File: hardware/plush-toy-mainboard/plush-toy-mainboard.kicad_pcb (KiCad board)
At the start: 4 copper layers, 90 x 60 mm, 108 parts, among them U1 ESP32-S3-WROOM-1-N16R8

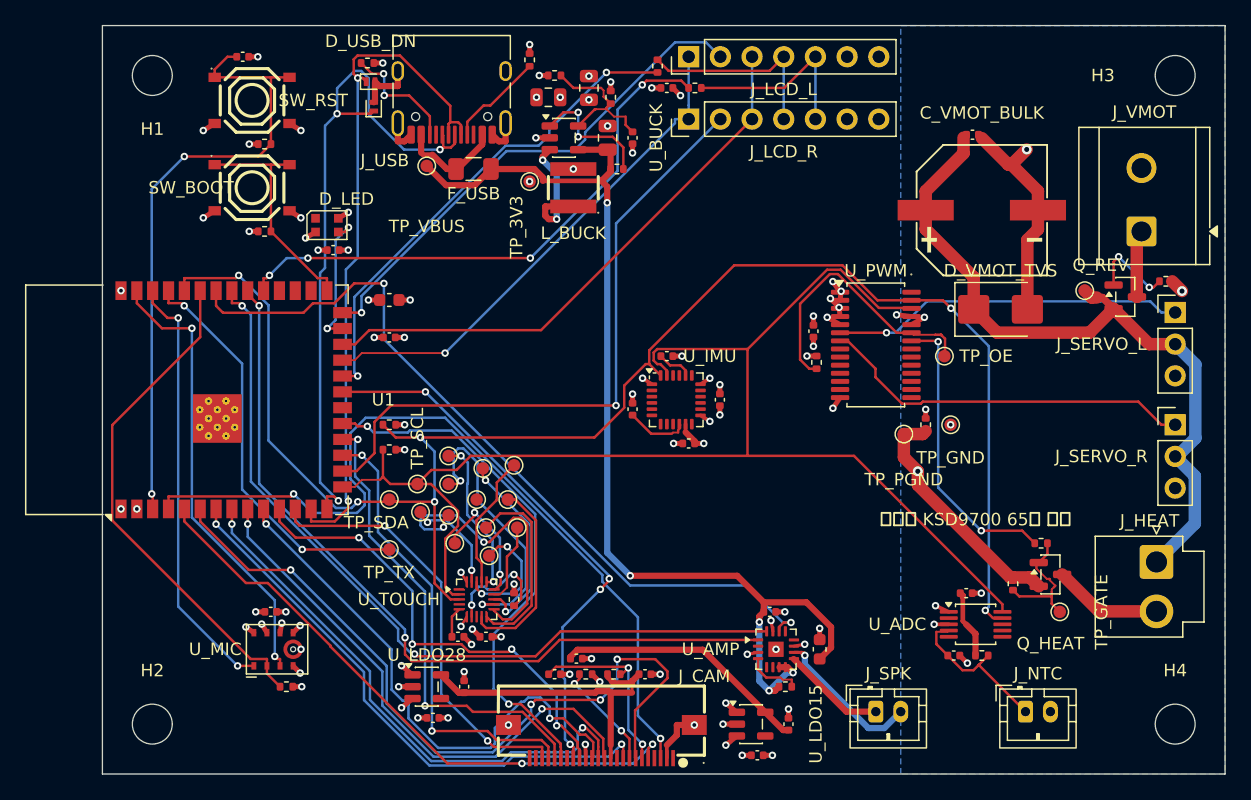
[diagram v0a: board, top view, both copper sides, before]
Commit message: feat(pcb): complete plush toy mainboard routing
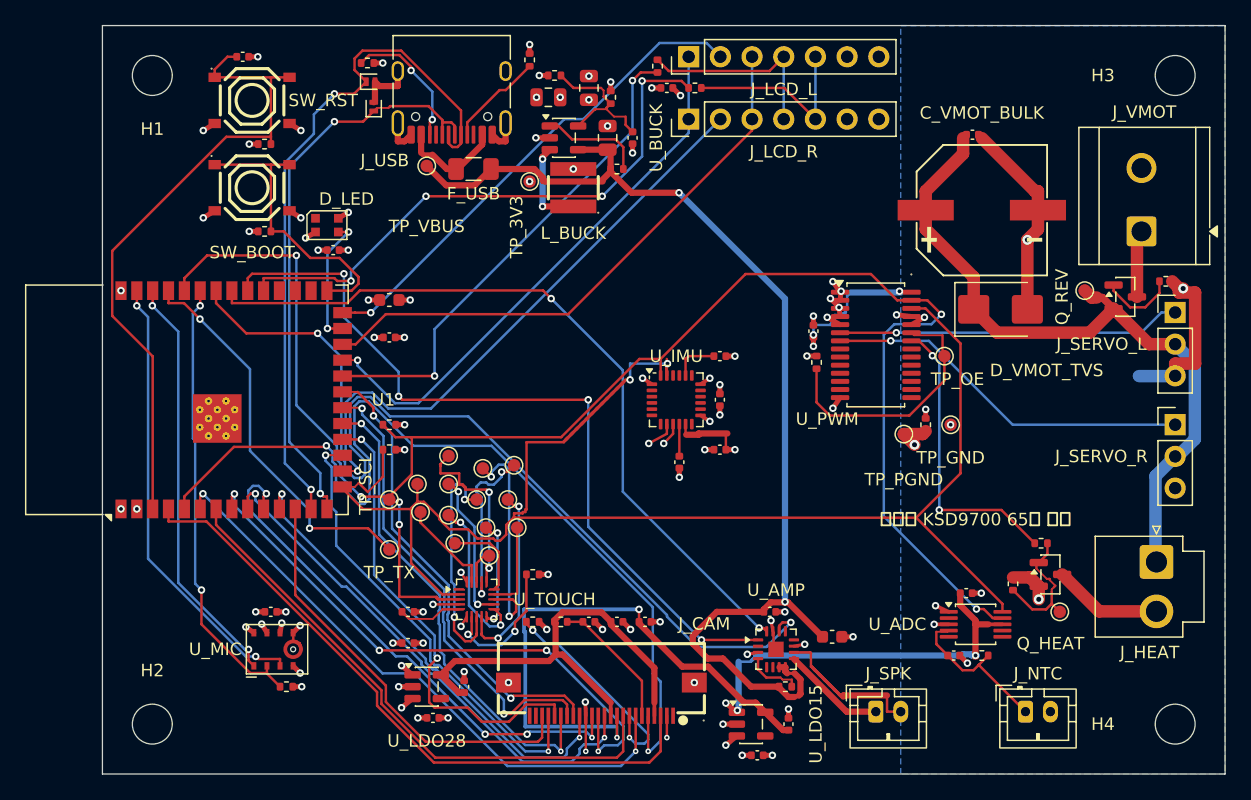
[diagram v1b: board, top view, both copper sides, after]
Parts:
- moved C_TOUCH 6.27 mm to (24.5, 49.5)
- moved C_CAM_DVDD 6.24 mm to (43.5, 47.8)
- moved R_CAM_PWDN 5.98 mm to (34.5, 47.8)
- moved R_CAM_RST 5.98 mm to (36.8, 47.8)
- moved C_IMU_REG 5.67 mm to (46.2, 35.0), turned to -90 degrees
- moved C_CAM_RST 5.02 mm to (39.0, 47.8)
- moved C_CAM_AVDD 4.76 mm to (41.2, 47.8)
- moved C_TOUCH_VREG 4.47 mm to (24.5, 47.0)
- moved C_IMU_CP 4.25 mm to (49.5, 26.5)
- moved J_CAM 3.40 mm to (40.0, 54.0)
- moved C_IMU_VLOGIC 2.55 mm to (49.5, 34.0)
- moved R_TOUCH_REXT 2.50 mm to (34.5, 44.0), turned to 0 degrees
- moved C_AMP_BULK 1.41 mm to (58.5, 49.0), turned to 0 degrees
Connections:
- D_LED pad 1: (no net) -> unconnected-(D_LED-DOUT-Pad1)
- J_CAM pad 1: (no net) -> unconnected-(J_CAM-Pad1)
- J_CAM pad 23: (no net) -> unconnected-(J_CAM-Pad23)
- J_CAM pad 24: (no net) -> unconnected-(J_CAM-Pad24)
- J_USB pad A8: (no net) -> unconnected-(J_USB-SBU1-PadA8)
- J_USB pad B8: (no net) -> unconnected-(J_USB-SBU2-PadB8)
- U1 pad 28: (no net) -> unconnected-(U1-IO35-Pad28)
- U1 pad 29: (no net) -> unconnected-(U1-IO36-Pad29)
- U1 pad 30: (no net) -> unconnected-(U1-IO37-Pad30)
- U_ADC pad 2: (no net) -> unconnected-(U_ADC-ALERT/RDY-Pad2)
- U_ADC pad 5: (no net) -> unconnected-(U_ADC-AIN1-Pad5)
- U_ADC pad 6: (no net) -> unconnected-(U_ADC-AIN2-Pad6)
- U_ADC pad 7: (no net) -> unconnected-(U_ADC-AIN3-Pad7)
- U_AMP pad 12: (no net) -> unconnected-(U_AMP-NC-Pad12)
- U_AMP pad 13: (no net) -> unconnected-(U_AMP-NC-Pad13)
- U_AMP pad 2: (no net) -> unconnected-(U_AMP-GAIN_SLOT-Pad2)
- U_AMP pad 5: (no net) -> unconnected-(U_AMP-NC-Pad5)
- U_AMP pad 6: (no net) -> unconnected-(U_AMP-NC-Pad6)
- U_IMU pad 12: (no net) -> unconnected-(U_IMU-INT-Pad12)
- U_IMU pad 14: (no net) -> unconnected-(U_IMU-NC-Pad14)
- U_IMU pad 15: (no net) -> unconnected-(U_IMU-NC-Pad15)
- U_IMU pad 16: (no net) -> unconnected-(U_IMU-NC-Pad16)
- U_IMU pad 17: (no net) -> unconnected-(U_IMU-NC-Pad17)
- U_IMU pad 19: (no net) -> unconnected-(U_IMU-RESV-Pad19)
- U_IMU pad 2: (no net) -> unconnected-(U_IMU-NC-Pad2)
- U_IMU pad 21: (no net) -> unconnected-(U_IMU-RESV-Pad21)
- U_IMU pad 22: (no net) -> unconnected-(U_IMU-RESV-Pad22)
- U_IMU pad 3: (no net) -> unconnected-(U_IMU-NC-Pad3)
- U_IMU pad 4: (no net) -> unconnected-(U_IMU-NC-Pad4)
- U_IMU pad 5: (no net) -> unconnected-(U_IMU-NC-Pad5)
- U_IMU pad 6: (no net) -> unconnected-(U_IMU-AUX_DA-Pad6)
- U_IMU pad 7: (no net) -> unconnected-(U_IMU-AUX_CL-Pad7)
- U_LDO15 pad 4: (no net) -> unconnected-(U_LDO15-NC-Pad4)
- U_LDO28 pad 4: (no net) -> unconnected-(U_LDO28-NC-Pad4)
- U_PWM pad 10: (no net) -> unconnected-(U_PWM-LED4-Pad10)
- U_PWM pad 11: (no net) -> unconnected-(U_PWM-LED5-Pad11)
- U_PWM pad 12: (no net) -> unconnected-(U_PWM-LED6-Pad12)
- U_PWM pad 13: (no net) -> unconnected-(U_PWM-LED7-Pad13)
- U_PWM pad 15: (no net) -> unconnected-(U_PWM-LED8-Pad15)
- U_PWM pad 16: (no net) -> unconnected-(U_PWM-LED9-Pad16)
- U_PWM pad 17: (no net) -> unconnected-(U_PWM-LED10-Pad17)
- U_PWM pad 18: (no net) -> unconnected-(U_PWM-LED11-Pad18)
- U_PWM pad 19: (no net) -> unconnected-(U_PWM-LED12-Pad19)
- U_PWM pad 20: (no net) -> unconnected-(U_PWM-LED13-Pad20)
- U_PWM pad 21: (no net) -> unconnected-(U_PWM-LED14-Pad21)
- U_PWM pad 8: (no net) -> unconnected-(U_PWM-LED2-Pad8)
- U_PWM pad 9: (no net) -> unconnected-(U_PWM-LED3-Pad9)
- U_TOUCH pad 1: (no net) -> unconnected-(U_TOUCH-~{IRQ}-Pad1)
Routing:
- net +3V3: track 27.1 -> 67.6 mm, vias 31 -> 36
- net CAM_Y6: track 0.00 -> 37.4 mm, vias 0 -> 2
- net CAM_SIOC: track 48.5 -> 74.9 mm
- net +1V5: track 20.5 -> 45.7 mm, vias 0 -> 2
- net TOUCH_E0: track 0.00 -> 18.7 mm, vias 0 -> 2
- net I2C_SCL: track 109.9 -> 124.7 mm, vias 0 -> 2
- net CAM_SIOD: track 66.5 -> 52.3 mm, vias 2 -> 0
- net CAM_VSYNC: track 61.0 -> 48.4 mm, vias 4 -> 2
- net AMP_LRCLK: track 63.8 -> 76.3 mm
- net GND: track 69.5 -> 81.2 mm, vias 70 -> 72
- net TOUCH_E3: track 24.2 -> 12.9 mm
- net +2V8: track 25.4 -> 36.3 mm
- net TOUCH_E4: track 22.7 -> 12.1 mm
- net USB_DP: track 55.6 -> 46.6 mm, vias 3 -> 2
- net CAM_PWDN: track 8.72 -> 17.6 mm
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
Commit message: fix(pcb): finalize plush toy preflight respin
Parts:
- removed TP_E0: TOUCH_E0, TestPoint:TestPoint_Pad_D1.0mm
- added C_BUCK_HF: 100nF, Capacitor_SMD:C_0402_1005Metric, F.Cu at (39.2, 16.5)
- added C_EFUSE_DVDT: 3.3nF, Capacitor_SMD:C_0402_1005Metric, F.Cu at (32.0, 21.5)
- added C_EFUSE_IN: 100nF, Capacitor_SMD:C_0402_1005Metric, F.Cu at (31.0, 19.2)
- added J_TOUCH: Head Touch, Connector_JST:JST_PH_B2B-PH-K_1x02_P2.00mm_Vertical, F.Cu at (19.0, 56.0)
- added R_EFUSE_ILM: 1.02k, Resistor_SMD:R_0402_1005Metric, F.Cu at (37.5, 18.8)
- added R_SIOC: 4.7k, Resistor_SMD:R_0402_1005Metric, F.Cu at (27.8, 57.0)
- added R_SIOD: 4.7k, Resistor_SMD:R_0402_1005Metric, F.Cu at (30.2, 57.0)
- added U_EFUSE: TPS259531DSGR, Package_SON:Texas_DSG0008A_WSON-8-1EP_2x2mm_P0.5mm_EP0.9x1.6mm_ThermalVias, F.Cu at (34.5, 19.0)
- D_LED: value WS2812B-2020 -> WS2812B-2020-V6
- moved C_EN 39.8 mm to (6.00, 42.0), turned to 90 degrees
- moved R_EN 33.6 mm to (4.50, 42.0), turned to 90 degrees
- moved C_U1_BULK 29.9 mm to (1.30, 42.5), turned to -90 degrees
- moved C_U1 26.2 mm to (3.00, 42.0), turned to -90 degrees
- moved TP_E8 17.6 mm to (43.0, 43.2)
- moved R_CC2 13.1 mm to (31.8, 10.8)
- moved R_CC1 12.9 mm to (21.5, 4.50), turned to 0 degrees
- moved C_BUCK_OUT2 12.5 mm to (42.5, 17.0), turned to 0 degrees
- moved C_BUCK_OUT1 11.3 mm to (43.5, 14.0), turned to 90 degrees
- moved TP_E9 9.86 mm to (40.0, 42.2)
- moved C_FF 9.78 mm to (41.8, 18.8), turned to 0 degrees
- moved TP_3V3 9.17 mm to (43.2, 10.8)
- moved F_USB 8.55 mm to (35.0, 4.75), turned to 90 degrees
- moved TP_E11 8.50 mm to (34.0, 39.0)
- moved R_BUCK_EN 7.11 mm to (40.0, 18.5), turned to 90 degrees
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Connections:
- F_USB pad 2: VBUS -> VBUS_FUSED
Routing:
- net CAM_Y6: track 37.4 -> 124.2 mm, vias 2 -> 13
- net GND: track 81.2 -> 149.2 mm, vias 72 -> 112
- net CAM_VSYNC: track 48.4 -> 74.6 mm
- net TOUCH_E7: track 6.95 -> 30.7 mm, vias 0 -> 2
- net CAM_SIOC: track 74.9 -> 52.8 mm, vias 2 -> 0
- net TOUCH_E6: track 7.18 -> 28.5 mm
- net VBUS_FUSED: track 0.00 -> 21.0 mm
- net +2V8: track 36.3 -> 57.2 mm, vias 0 -> 4
- net CAM_Y7: track 37.7 -> 58.0 mm
- net CAM_Y8: track 41.7 -> 61.7 mm, vias 4 -> 2
- net PGND: track 37.2 -> 57.2 mm, vias 4 -> 6
- net I2C_SCL: track 124.7 -> 104.9 mm, vias 2 -> 0
- net CAM_HREF: track 45.3 -> 64.6 mm, vias 0 -> 4
- net CAM_RESET: track 10.7 -> 26.5 mm, vias 0 -> 2
- net CAM_PCLK: track 37.2 -> 52.5 mm, vias 2 -> 4
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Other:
- board text added: "+"
- board text added: "-"
- board text added: "CH0 左"
- board text added: "CH1 右"
- board text added: "VMOT 仅限 5V"
- board text added: "头部触摸 E0 / GND"
- board text added: "电机/加热专用 5V"
